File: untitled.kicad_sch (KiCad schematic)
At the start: 88 parts, among them J10 PINHD_1x3_Male, J11 PINHD_1x3_Male, J12 PINHD_1x4_Male, J13 PINHD_1x3_Male, J14 PINHD_1x3_Male, J15 PINHD_1x4_Male, J3 PINHD_1x4_Male, J4 PINHD_1x3_Male, J5 PINHD_1x3_Male, J7 PINHD_1x3_Male, J8 PINHD_1x3_Male, J9 PINHD_1x4_Male, U2 DRV8825PWP, U3 DRV8825PWP, U4 DRV8825PWP, U5 DRV8825PWP

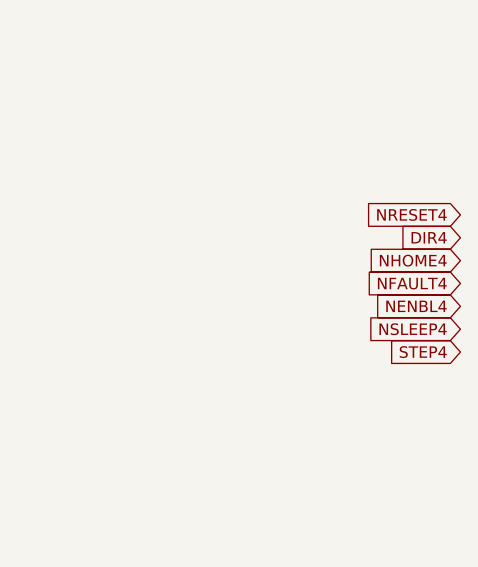
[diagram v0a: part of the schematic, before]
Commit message: cleaned up main schematic
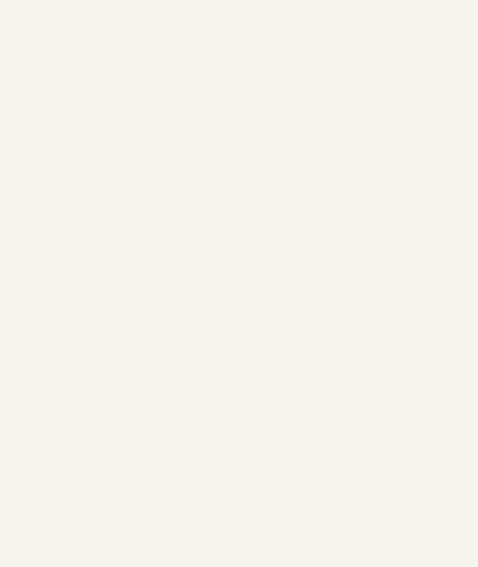
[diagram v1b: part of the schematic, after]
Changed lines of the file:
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@@
-    )
-  )
-  (global_label "NENBL4" (shape input) (at 328.295 151.13 180) (fields_autoplaced)
-    (effects (font (size 1.27 1.27)) (justify right))
-    (property "Intersheetrefs" "${INTERSHEET_REFS}" (at 317.9922 151.13 0)
-      (effects (font (size 1.27 1.27)) (justify right) hide)
     )
   )
@@
     )
   )
-  (global_label "STEP4" (shape input) (at 328.295 156.21 180) (fields_autoplaced)
-    (effects (font (size 1.27 1.27)) (justify right))
-    (property "Intersheetrefs" "${INTERSHEET_REFS}" (at 319.5042 156.21 0)
-      (effects (font (size 1.27 1.27)) (justify right) hide)
-    )
-  )
   (global_label "STEP1" (shape input) (at 77.47 59.69 180) (fields_autoplaced)
     (effects (font (size 1.27 1.27)) (justify right))
@@
     )
   )
-  (global_label "DIR4" (shape input) (at 328.295 143.51 180) (fields_autoplaced)
-    (effects (font (size 1.27 1.27)) (justify right))
-    (property "Intersheetrefs" "${INTERSHEET_REFS}" (at 320.9555 143.51 0)
-      (effects (font (size 1.27 1.27)) (justify right) hide)
-    )
-  )
   (global_label "VM" (shape input) (at 114.3 19.05 180) (fields_autoplaced)
     (effects (font (size 1.27 1.27)) (justify right))
@@
     )
   )
-  (global_label "NSLEEP4" (shape input) (at 328.295 153.67 180) (fields_autoplaced)
-    (effects (font (size 1.27 1.27)) (justify right))
-    (property "Intersheetrefs" "${INTERSHEET_REFS}" (at 316.9642 153.67 0)
-      (effects (font (size 1.27 1.27)) (justify right) hide)
-    )
-  )
   (global_label "VREF4" (shape input) (at 250.825 53.34 0) (fields_autoplaced)
     (effects (font (size 1.27 1.27)) (justify left))
@@
     )
   )
-  (global_label "NRESET4" (shape input) (at 328.295 140.97 180) (fields_autoplaced)
-    (effects (font (size 1.27 1.27)) (justify right))
-    (property "Intersheetrefs" "${INTERSHEET_REFS}" (at 317.0247 140.97 0)
-      (effects (font (size 1.27 1.27)) (justify right) hide)
-    )
-  )
   (global_label "VM" (shape input) (at 140.335 151.13 270) (fields_autoplaced)
     (effects (font (size 1.27 1.27)) (justify right))
@@
     )
   )
-  (global_label "NFAULT4" (shape input) (at 328.295 148.59 180) (fields_autoplaced)
-    (effects (font (size 1.27 1.27)) (justify right))
-    (property "Intersheetrefs" "${INTERSHEET_REFS}" (at 317.2664 148.59 0)
-      (effects (font (size 1.27 1.27)) (justify right) hide)
-    )
-  )
   (global_label "NSLEEP3" (shape input) (at 144.78 111.76 180) (fields_autoplaced)
     (effects (font (size 1.27 1.27)) (justify right))
@@
       (effects (font (size 1.27 1.27)) (justify right) hide)
     )
-  )
-  (global_label "NHOME4" (shape input) (at 328.295 146.05 180) (fields_autoplaced)
-    (effects (font (size 1.27 1.27)) (justify right))
-    (property "Intersheetrefs" "${INTERSHEET_REFS}" (at 317.5084 146.05 0)
-      (effects (font (size 1.27 1.27)) (justify right) hide)
-    )
